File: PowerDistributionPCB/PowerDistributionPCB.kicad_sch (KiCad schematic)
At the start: 40 parts, among them J1 USB3_A, Q1 AOD4185, U1 AP63203WU

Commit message: fixed buck converter footprint
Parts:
- 12V1, 5V1: footprint CUSail:TPSM84338RCJR -> CUSail:buck_correct
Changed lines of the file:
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@@
 			)
 		)
-		(property "Footprint" "CUSail:TPSM84338RCJR"
+		(property "Footprint" "CUSail:buck_correct"
 			(at 182.88 130.81 0)
 			(effects
@@
 			)
 		)
-		(property "Footprint" "CUSail:TPSM84338RCJR"
+		(property "Footprint" "CUSail:buck_correct"
 			(at 185.42 80.01 0)
 			(effects

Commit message: fixed resistor/capacitor sizes
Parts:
- C2a1, C2b1: footprint Capacitor_SMD:C_01005_0402Metric_Pad0.57x0.30mm_HandSolder -> Capacitor_SMD:C_0201_0603Metric_Pad0.64x0.40mm_HandSolder
- Rfbb1, Rfbb2, Rfbt1, Rfbt2: footprint Capacitor_SMD:C_01005_0402Metric_Pad0.57x0.30mm_HandSolder -> Resistor_SMD:R_0201_0603Metric_Pad0.64x0.40mm_HandSolder
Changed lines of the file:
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@@
 			)
 		)
-		(property "Footprint" "Capacitor_SMD:C_01005_0402Metric_Pad0.57x0.30mm_HandSolder"
+		(property "Footprint" "Resistor_SMD:R_0201_0603Metric_Pad0.64x0.40mm_HandSolder"
 			(at 233.172 106.68 90)
 			(effects
@@
 			)
 		)
-		(property "Footprint" "Capacitor_SMD:C_01005_0402Metric_Pad0.57x0.30mm_HandSolder"
+		(property "Footprint" "Capacitor_SMD:C_0201_0603Metric_Pad0.64x0.40mm_HandSolder"
 			(at 160.9852 147.32 0)
 			(effects
@@
 			)
 		)
-		(property "Footprint" "Capacitor_SMD:C_01005_0402Metric_Pad0.57x0.30mm_HandSolder"
+		(property "Footprint" "Resistor_SMD:R_0201_0603Metric_Pad0.64x0.40mm_HandSolder"
 			(at 240.792 149.86 90)
 			(effects
@@
 			)
 		)
-		(property "Footprint" "Capacitor_SMD:C_01005_0402Metric_Pad0.57x0.30mm_HandSolder"
+		(property "Footprint" "Capacitor_SMD:C_0201_0603Metric_Pad0.64x0.40mm_HandSolder"
 			(at 167.3352 100.33 0)
 			(effects
@@
 			)
 		)
-		(property "Footprint" "Capacitor_SMD:C_01005_0402Metric_Pad0.57x0.30mm_HandSolder"
+		(property "Footprint" "Resistor_SMD:R_0201_0603Metric_Pad0.64x0.40mm_HandSolder"
 			(at 229.362 88.9 90)
 			(effects
@@
 			)
 		)
-		(property "Footprint" "Capacitor_SMD:C_01005_0402Metric_Pad0.57x0.30mm_HandSolder"
+		(property "Footprint" "Resistor_SMD:R_0201_0603Metric_Pad0.64x0.40mm_HandSolder"
 			(at 240.792 138.43 90)
 			(effects

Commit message: update layout, adjust relay connections/footprint
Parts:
- Cout1, Cout2, Cout3: footprint Capacitor_SMD:C_1210_3225Metric_Pad1.33x2.70mm_HandSolder -> Capacitor_SMD:C_1206_3216Metric_Pad1.33x1.80mm_HandSolder
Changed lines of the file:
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@@
 			)
 		)
-		(property "Footprint" "Capacitor_SMD:C_1210_3225Metric_Pad1.33x2.70mm_HandSolder"
+		(property "Footprint" "Capacitor_SMD:C_1206_3216Metric_Pad1.33x1.80mm_HandSolder"
 			(at 262.5852 147.32 0)
 			(effects
@@
 			)
 		)
-		(property "Footprint" "Capacitor_SMD:C_1210_3225Metric_Pad1.33x2.70mm_HandSolder"
+		(property "Footprint" "Capacitor_SMD:C_1206_3216Metric_Pad1.33x1.80mm_HandSolder"
 			(at 253.6952 147.32 0)
 			(effects
@@
 			)
 		)
-		(property "Footprint" "Capacitor_SMD:C_1210_3225Metric_Pad1.33x2.70mm_HandSolder"
+		(property "Footprint" "Capacitor_SMD:C_1206_3216Metric_Pad1.33x1.80mm_HandSolder"
 			(at 272.7452 147.32 0)
 			(effects

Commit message: updated buck layout traces
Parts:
- Main_Bulk(electrolytic)1: footprint Capacitor_SMD:C_0201_0603Metric_Pad0.64x0.40mm_HandSolder -> Capacitor_SMD:C_1210_3225Metric_Pad1.33x2.70mm_HandSolder
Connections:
- net GND: now also 12V1.9 (RT_SYNC)
- no-connect marks 43 -> 42
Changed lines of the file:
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@@
 	)
 	(junction
+		(at 166.37 160.02)
+		(diameter 0)
+		(color 0 0 0 0)
+	)
+	(junction
 		(at 21.59 123.19)
 		(diameter 0)
@@
 	)
 	(no_connect
-		(at 182.88 142.24)
-	)
-	(no_connect
 		(at 111.76 146.05)
 	)
@@
 	(wire
 		(pts
+			(xy 182.88 142.24) (xy 173.99 142.24)
+		)
+		(stroke
+			(width 0)
+			(type default)
+		)
+	)
+	(wire
+		(pts
 			(xy 223.52 142.24) (xy 242.57 142.24)
 		)
@@
 	(wire
 		(pts
+			(xy 166.37 149.86) (xy 166.37 160.02)
+		)
+		(stroke
+			(width 0)
+			(type default)
+		)
+	)
+	(wire
+		(pts
 			(xy 226.06 86.36) (xy 226.06 82.55)
 		)
@@
 	(wire
 		(pts
+			(xy 173.99 142.24) (xy 166.37 149.86)
+		)
+		(stroke
+			(width 0)
+			(type default)
+		)
+	)
+	(wire
+		(pts
 			(xy 261.62 134.62) (xy 261.62 139.7)
 		)
@@
 	(wire
 		(pts
+			(xy 166.37 160.02) (xy 160.02 160.02)
+		)
+		(stroke
+			(width 0)
+			(type default)
+		)
+	)
+	(wire
+		(pts
 			(xy 82.55 46.99) (xy 83.82 46.99)
 		)
@@
 	(wire
 		(pts
-			(xy 171.45 160.02) (xy 160.02 160.02)
+			(xy 171.45 160.02) (xy 166.37 160.02)
 		)
 		(stroke
@@
 			)
 		)
-		(property "Footprint" "Capacitor_SMD:C_0201_0603Metric_Pad0.64x0.40mm_HandSolder"
+		(property "Footprint" "Capacitor_SMD:C_1210_3225Metric_Pad1.33x2.70mm_HandSolder"
 			(at 201.6252 30.48 0)
 			(effects

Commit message: updated buck layout and edge cuts
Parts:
- C2, C3, C4: footprint Capacitor_SMD:C_0201_0603Metric_Pad0.64x0.40mm_HandSolder -> Capacitor_SMD:C_0603_1608Metric_Pad1.08x0.95mm_HandSolder
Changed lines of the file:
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@@
 			)
 		)
-		(property "Footprint" "Capacitor_SMD:C_0201_0603Metric_Pad0.64x0.40mm_HandSolder"
+		(property "Footprint" "Capacitor_SMD:C_0603_1608Metric_Pad1.08x0.95mm_HandSolder"
 			(at 164.7952 184.15 0)
 			(effects
@@
 			)
 		)
-		(property "Footprint" "Capacitor_SMD:C_0201_0603Metric_Pad0.64x0.40mm_HandSolder"
+		(property "Footprint" "Capacitor_SMD:C_0603_1608Metric_Pad1.08x0.95mm_HandSolder"
 			(at 140.97 173.0248 0)
 			(effects
@@
 			)
 		)
-		(property "Footprint" "Capacitor_SMD:C_0201_0603Metric_Pad0.64x0.40mm_HandSolder"
+		(property "Footprint" "Capacitor_SMD:C_0603_1608Metric_Pad1.08x0.95mm_HandSolder"
 			(at 154.6352 184.15 0)
 			(effects

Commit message: fixing relay stuff
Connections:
- net 12VBuck: no longer A1.30 (VIN)
- net 5VSafe: no longer names the net of A1.27 (+5V)
- no-connect marks 42 -> 43
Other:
- moved on the sheet: A1

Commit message: final updates to schematic and layout connections
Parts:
- added C5: 470u, Capacitor_SMD:CP_Elec_8x10.5, symbol Device:C_Polarized
- added D9: SS14, Diode_SMD:D_SMA, symbol Diode:SS14
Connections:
- net 5VBuck: now also D9.2 (A)
- net GND: now also C5.2
- net at A1.27 (+5V): now also C5.1, D9.1 (K)

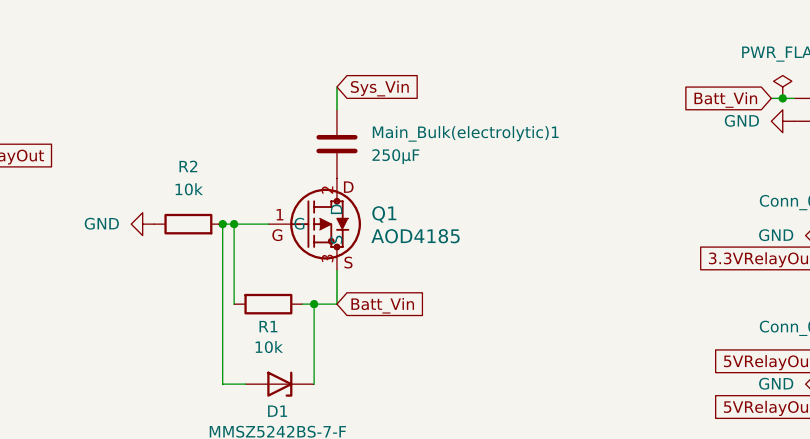
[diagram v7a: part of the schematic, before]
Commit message: updated battery protection capacitor
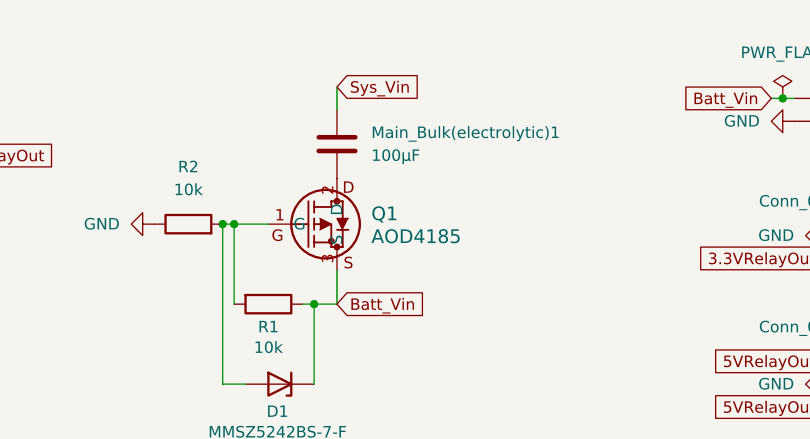
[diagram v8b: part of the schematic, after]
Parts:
- Main_Bulk(electrolytic)1: value 250µF -> 100µF
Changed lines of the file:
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@@
 			)
 		)
-		(property "Value" "250µF"
+		(property "Value" "100µF"
 			(at 204.47 27.9399 0)
 			(effects
